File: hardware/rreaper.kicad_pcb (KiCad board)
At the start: 2 copper layers, 20 parts, among them J1 ZIF, J2 USB_B_Micro, J3 ICP, U1 ATmega328P, U2 MCP2221A, U3 74HC595, U4 74HC595, X1 16MHz

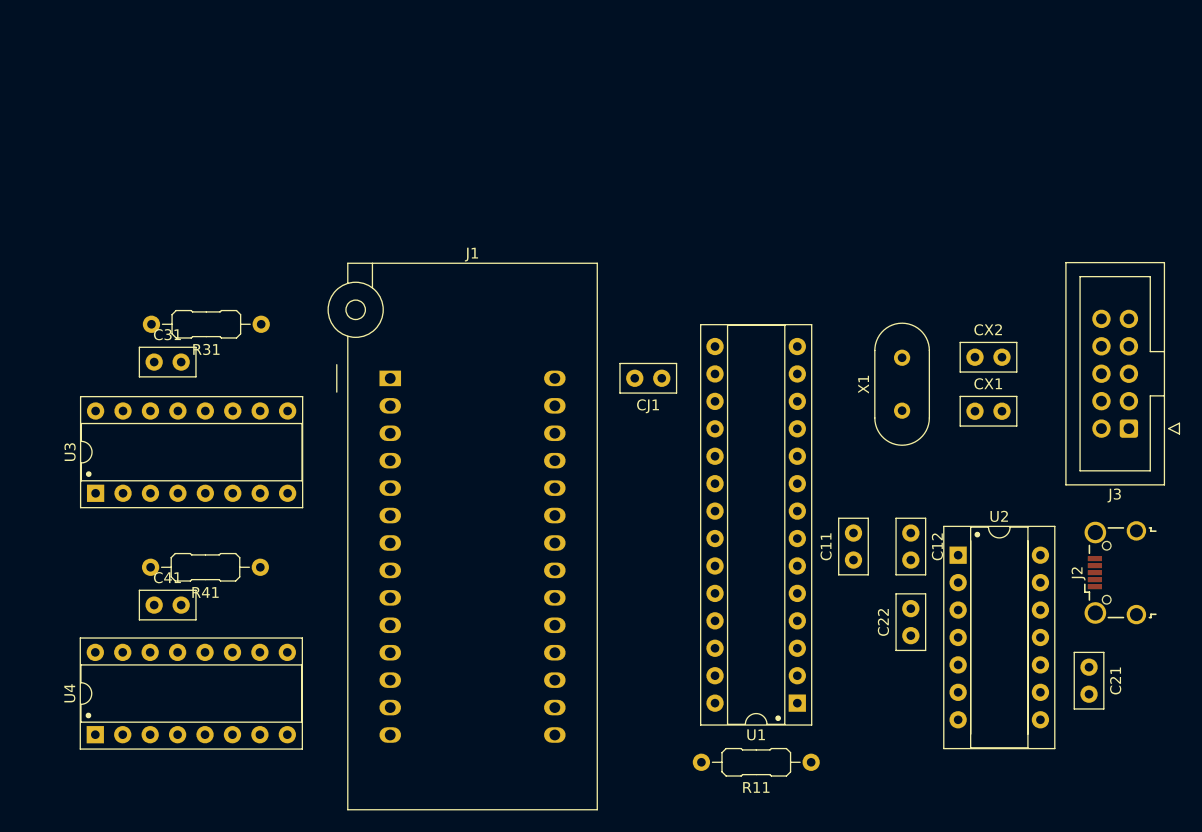
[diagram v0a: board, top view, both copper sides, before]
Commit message: completed first PCB layout
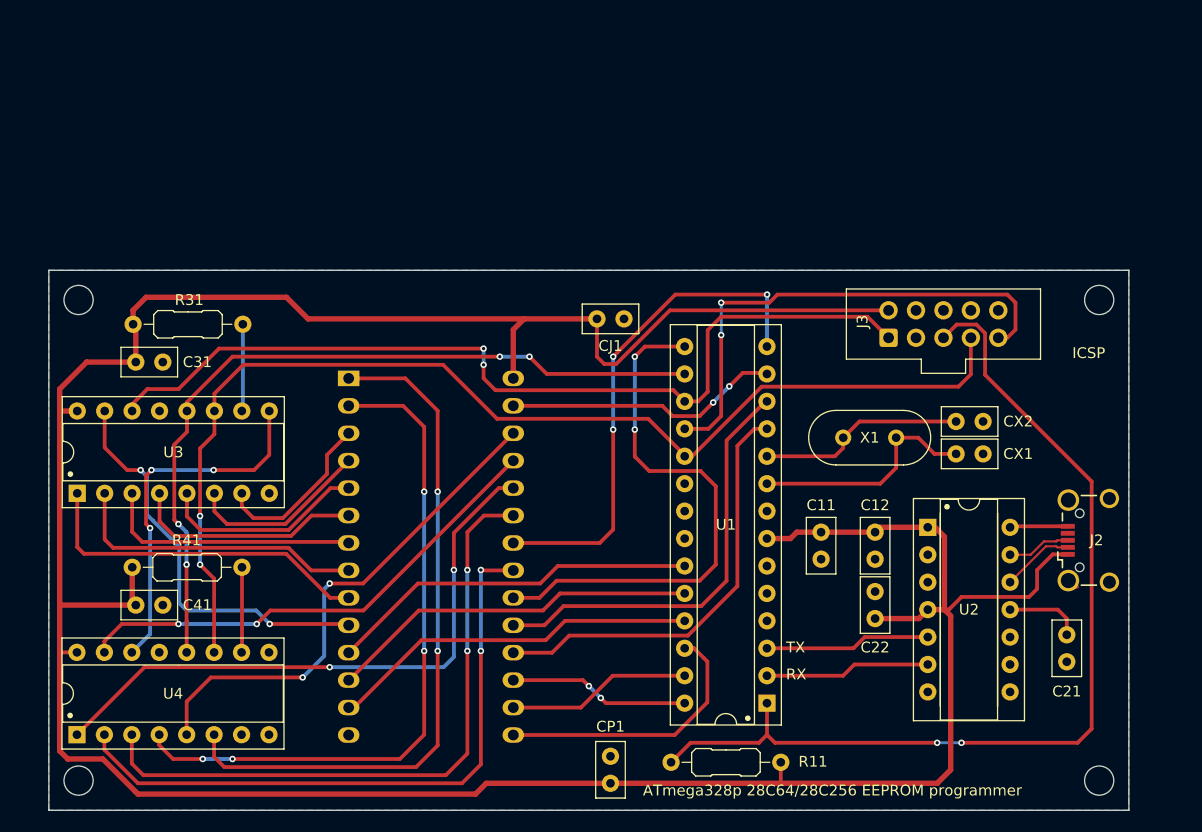
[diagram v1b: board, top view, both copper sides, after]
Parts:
- added CP1: 1u, Capacitor_THT:C_Disc_D5.0mm_W2.5mm_P2.50mm, F.Cu at (129.5, 118.0)
- added H1: MountingHole, MountingHole:MountingHole_2.7mm_M2.5, F.Cu at (174.8, 75.8)
- added H2: MountingHole, MountingHole:MountingHole_2.7mm_M2.5, F.Cu at (174.8, 120.2)
- added H3: MountingHole, MountingHole:MountingHole_2.7mm_M2.5, F.Cu at (80.2, 120.2)
- added H4: MountingHole, MountingHole:MountingHole_2.7mm_M2.5, F.Cu at (80.2, 75.8)
- J3: value ICP -> ICSP
- moved J3 23.8 mm to (155.2, 79.2), turned to 90 degrees
- moved CJ1 6.52 mm to (130.8, 77.5)
- moved CX2 6.20 mm to (161.5, 87.0)
- moved CX1 4.32 mm to (161.5, 90.0)
- moved C11 3.96 mm to (149.0, 97.2), turned to -90 degrees
- moved J2 3.91 mm to (173.7, 98.0)
- moved J1 3.85 mm to (105.3, 83.0)
- moved U2 3.81 mm to (158.9, 96.8)
- moved C22 3.67 mm to (154.0, 105.2)
- moved C21 3.64 mm to (171.8, 106.8)
- moved C12 3.31 mm to (154.0, 97.2)
- moved R11 2.81 mm to (145.3, 118.6)
- moved U1 2.81 mm to (144.0, 113.1)
- moved X1 2.56 mm to (155.9, 88.5), turned to 180 degrees
- moved C31 1.70 mm to (85.5, 81.5)
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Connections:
- net Net-(J2-D+) renamed /USB+
- net Net-(J2-D-) renamed /USB-
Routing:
- net +5V: track 0.00 -> 291.0 mm
- net SCK: track 0.00 -> 106.3 mm, vias 0 -> 2
- net ~{RST}: track 0.00 -> 89.2 mm, vias 0 -> 2
- net MOSI: track 0.00 -> 83.8 mm, vias 0 -> 2
- net LATCH: track 0.00 -> 72.6 mm, vias 0 -> 4
- net A14: track 0.00 -> 64.5 mm, vias 0 -> 2
- net A12: track 0.00 -> 63.3 mm, vias 0 -> 4
- net A11: track 0.00 -> 60.4 mm, vias 0 -> 2
- net A10: track 0.00 -> 59.3 mm, vias 0 -> 2
- net A9: track 0.00 -> 56.6 mm, vias 0 -> 2
- net CE: track 0.00 -> 50.2 mm, vias 0 -> 2
- net A13: track 0.00 -> 47.2 mm, vias 0 -> 2
- net OE: track 0.00 -> 47.2 mm, vias 0 -> 3
- net MISO: track 0.00 -> 46.6 mm, vias 0 -> 2
- net A8: track 0.00 -> 45.8 mm, vias 0 -> 2
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- added copper zone on B.Cu, net GND
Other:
- board outline added: 100 x 50 mm
- board text added: "ATmega328p 28C64/28C256 EEPROM programmer"
- board text added: "ICSP"
- board text added: "RX"
- board text added: "TX"

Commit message: hardware: replaced USB with RS485 and external power; redesigned PCB
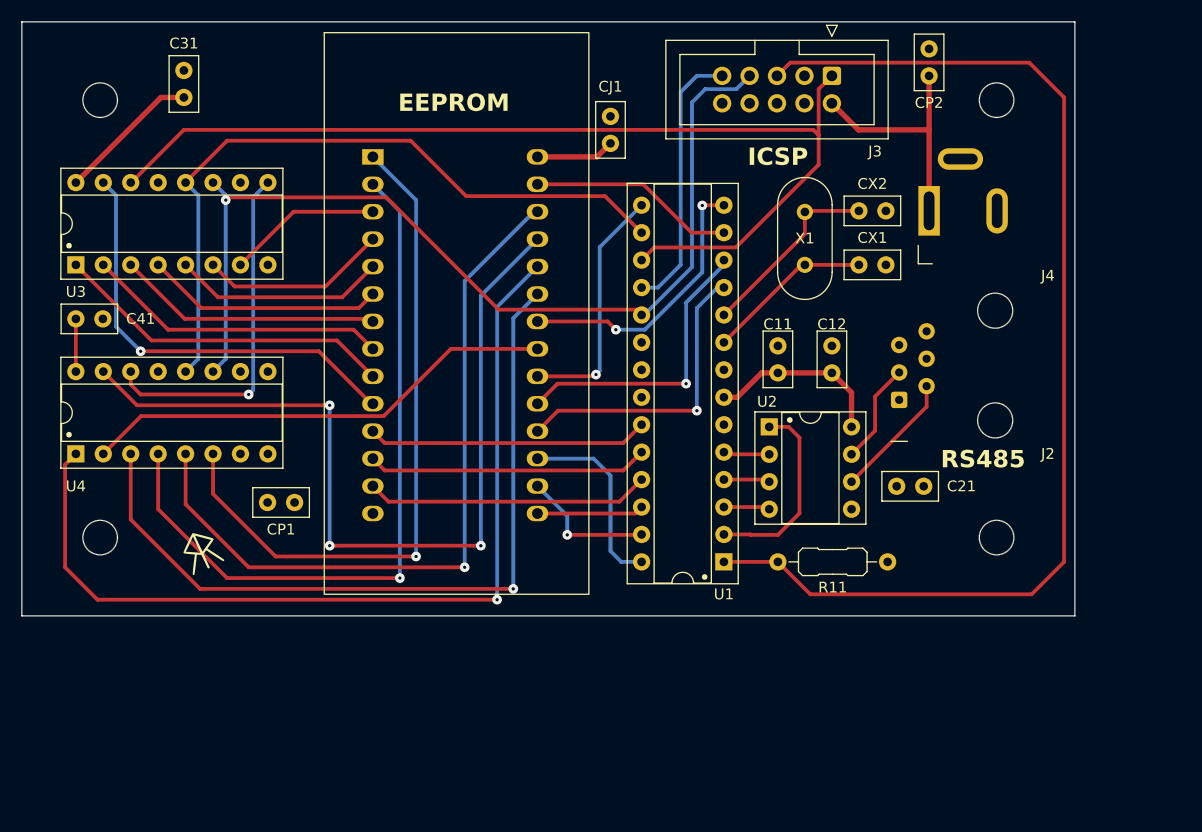
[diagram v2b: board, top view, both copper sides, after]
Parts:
- removed C22: 100n, Capacitor_THT:C_Disc_D5.0mm_W2.5mm_P2.50mm
- removed R31, R41: 4k7, PCM_Resistor_THT_AKL:R_Axial_DIN0207_L6.3mm_D2.5mm_P10.16mm_Horizontal
- added CP2: 1u, Capacitor_THT:C_Disc_D5.0mm_W2.5mm_P2.50mm, F.Cu at (159.0, 52.5)
- added G***: LOGO, LOGO, F.Cu at (91.5, 99.0)
- added G***: LOGO, LOGO, B.Cu at (127.0, 52.5)
- added J4: 5V_{DC}, Connector_BarrelJack:BarrelJack_GCT_DCJ200-10-A_Horizontal, F.Cu at (159.0, 67.5)
- C21: value 220n -> 100n
- H1, H2, H3, H4: footprint MountingHole:MountingHole_2.7mm_M2.5 -> MountingHole:MountingHole_3.2mm_M3
- J2: value USB_B_Micro -> RS485; footprint Connector_USB:USB_Micro-B_Wuerth_629105150521_CircularHoles -> Connector_RJ:RJ12_Amphenol_54601-x06_Horizontal
- U2: value MCP2221A -> SN75176AP; footprint PCM_Package_DIP_AKL:DIP-14_W7.62mm_Socket -> PCM_Package_DIP_AKL:DIP-8_W7.62mm_Socket
- moved H2 95.2 mm to (82.2, 97.8)
- moved H1 94.3 mm to (82.2, 57.2)
- moved H3 87.9 mm to (165.2, 97.8)
- moved H4 87.0 mm to (165.2, 57.2)
- moved CP1 37.5 mm to (100.2, 94.5), turned to 180 degrees
- moved C41 27.1 mm to (80.0, 77.5)
- moved U4 26.0 mm to (80.0, 90.0)
- moved C31 24.9 mm to (90.0, 57.0), turned to 90 degrees
- moved J3 24.8 mm to (150.0, 55.0), turned to -90 degrees
- moved J2 21.8 mm to (156.2, 85.0)
- moved CX2 21.5 mm to (152.5, 67.5)
- moved U3 21.2 mm to (80.0, 72.5)
- moved R11 21.0 mm to (155.2, 100.0)
- moved C21 20.9 mm to (156.0, 93.0), turned to 0 degrees
- moved J1 20.6 mm to (107.5, 62.5)
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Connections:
- C21 pad 1: Net-(U2-VUSB) -> +5V
- J2 pad 1: +5V -> GND
- J2 pad 2: /USB- -> SA
- J2 pad 3: /USB+ -> SB
- J2 pad 5: GND -> unconnected-(J2-Pad5)
- U1 pad 2: UART_{PC->MCU} -> RX
- U1 pad 3: UART_{MCU->PC} -> TX
- U1 pad 4: unconnected-(U1-PD2-Pad4) -> DE
- U1 pad 5: unconnected-(U1-PD3-Pad5) -> ~{RE}
- U2 pad 1: +5V -> RX
- U2 pad 2: unconnected-(U2-GP0-Pad2) -> ~{RE}
- U2 pad 3: unconnected-(U2-GP1-Pad3) -> DE
- U2 pad 4: +5V -> TX
- U2 pad 5: UART_{MCU->PC} -> GND
- U2 pad 6: UART_{PC->MCU} -> SA
- U2 pad 7: unconnected-(U2-GP2-Pad7) -> SB
- U2 pad 8: unconnected-(U2-GP3-Pad8) -> +5V
- U3 pad 10: Net-(U3-~{SRCLR}) -> +5V
- U4 pad 10: Net-(U4-~{SRCLR}) -> +5V
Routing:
- net +5V: track 291.0 -> 64.6 mm
- net A8: track 45.8 -> 79.8 mm, vias 2 -> 3
- net A9: track 56.6 -> 84.7 mm, vias 2 -> 1
- net CE: track 50.2 -> 22.9 mm, vias 2 -> 1
- net MISO: track 46.6 -> 24.9 mm, vias 2 -> 0
- net A13: track 47.2 -> 68.8 mm, vias 2 -> 1
- net OE: track 47.2 -> 26.0 mm, vias 3 -> 2
- net RX: track 0.00 -> 18.1 mm
- net SCK: track 106.3 -> 89.6 mm, vias 2 -> 1
- net ~{RST}: track 89.2 -> 105.4 mm, vias 2 -> 0
- net D3: track 25.6 -> 9.89 mm
- net UART_{MCU->PC}: track 15.6 -> 0.00 mm
- net UART_{PC->MCU}: track 15.3 -> 0.00 mm
- net A10: track 59.3 -> 44.2 mm, vias 2 -> 0
- net D7: track 39.7 -> 27.4 mm, vias 0 -> 1
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- added copper zone on In1.Cu, net +5V
- added copper zone on In2.Cu, net GND
- removed copper zone on B.Cu, net GND
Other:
- board size 100 x 50 mm -> 97.5 x 55 mm
- copper layers 2 -> 4
- board text added: "5V"
- board text added: "COMPATIBLE DEVICES: AT28C64 AT28C256"
- board text added: "EEPROM"
- board text added: "RS485"
- board text added: "RS485: 1 GND 2 A 3 B ... X"
- board text removed: "ATmega328p 28C64/28C256 EEPROM programmer"
- board text removed: "RX"
- board text removed: "TX"

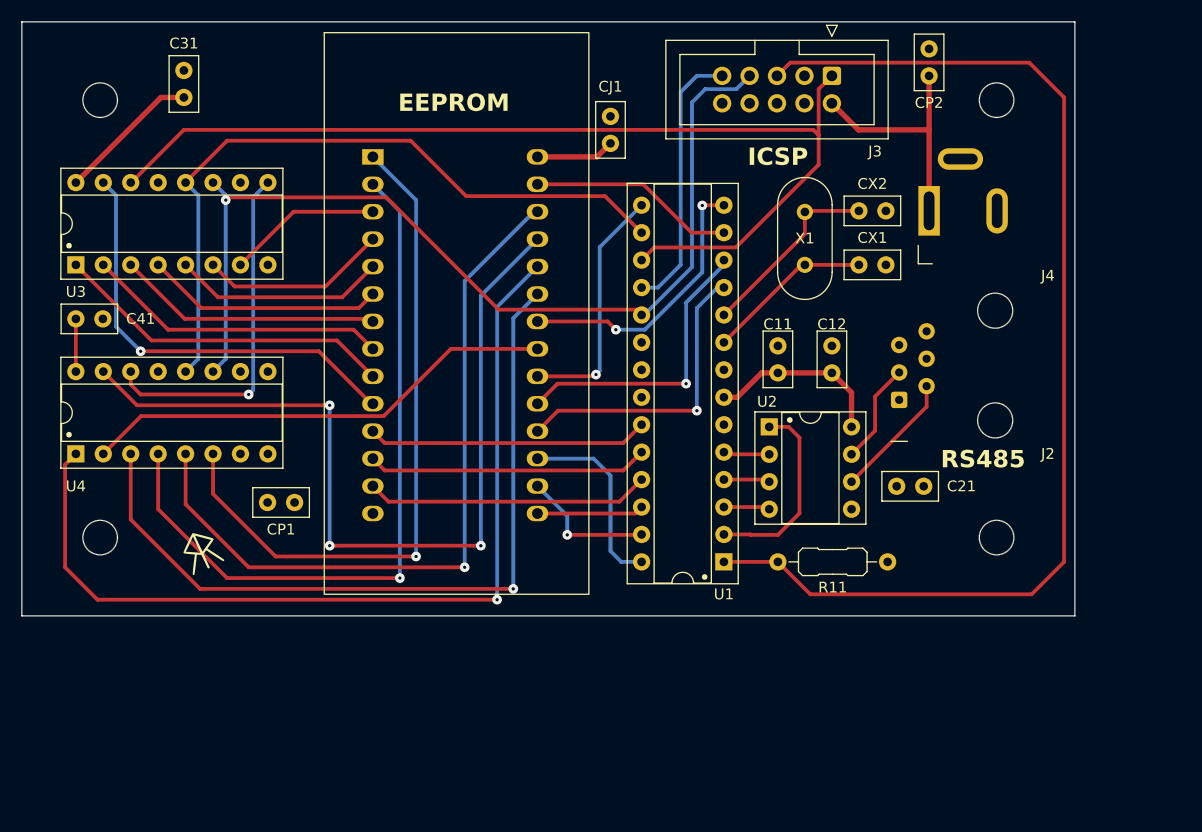
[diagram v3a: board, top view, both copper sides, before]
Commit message: went back to USB; added serial eeprom socket; completed new layout
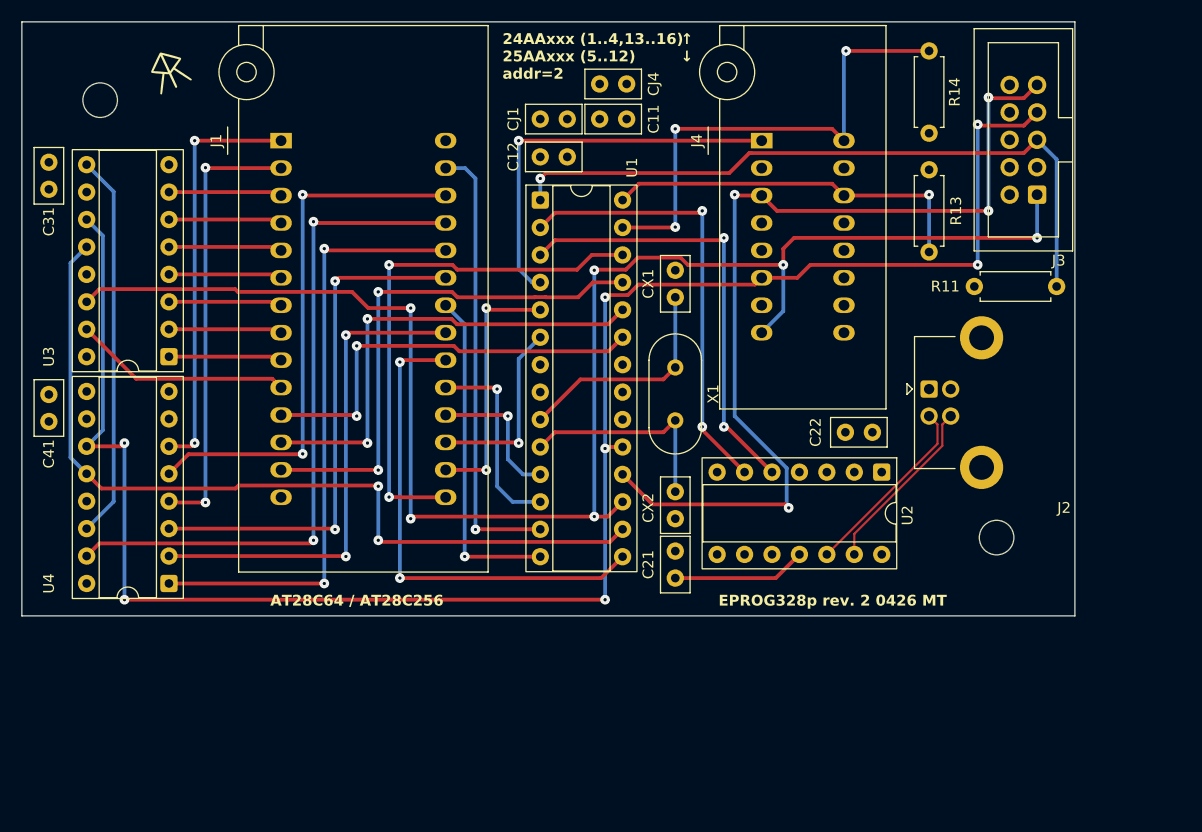
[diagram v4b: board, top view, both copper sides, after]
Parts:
- removed CP1, CP2: 1u, Capacitor_THT:C_Disc_D5.0mm_W2.5mm_P2.50mm
- removed the G*** at (127.0, 52.5)
- removed H2, H4: MountingHole, MountingHole:MountingHole_3.2mm_M3
- added C22: 100n, Capacitor_THT:C_Disc_D5.0mm_W2.5mm_P2.50mm, F.Cu at (153.8, 88.0)
- added CJ4: 100n, Capacitor_THT:C_Disc_D5.0mm_W2.5mm_P2.50mm, F.Cu at (131.0, 55.8)
- added R13: 4k7, Resistor_THT:R_Axial_DIN0207_L6.3mm_D2.5mm_P7.62mm_Horizontal, F.Cu at (159.0, 71.3)
- added R14: 4k7, Resistor_THT:R_Axial_DIN0207_L6.3mm_D2.5mm_P7.62mm_Horizontal, F.Cu at (159.0, 52.7)
- C21: value 100n -> 220n
- J1: value ZIF -> ZIF28; footprint Socket:DIP_Socket-28_W11.9_W12.7_W15.24_W17.78_W18.5_3M_228-1277-00-0602J -> Socket:DIP_Socket-28_W11.9mm_W12.7mm_W15.24mm_W17.78mm_W18.5mm_3M_228-1277-00-0602J
- J2: value RS485 -> USB_B; footprint Connector_RJ:RJ12_Amphenol_54601-x06_Horizontal -> Connector_USB:USB_B_Lumberg_2411_02_Horizontal
- J4: value 5V_{DC} -> ZIF16; footprint Connector_BarrelJack:BarrelJack_GCT_DCJ200-10-A_Horizontal -> Socket:DIP_Socket-16_W4.3mm_W5.08mm_W7.62mm_W10.16mm_W10.9mm_3M_216-3340-00-0602J
- R11: footprint PCM_Resistor_THT_AKL:R_Axial_DIN0207_L6.3mm_D2.5mm_P10.16mm_Horizontal -> Resistor_THT:R_Axial_DIN0207_L6.3mm_D2.5mm_P7.62mm_Horizontal
- U1: footprint PCM_Package_DIP_AKL:DIP-28_W7.62mm_Socket -> Package_DIP:DIP-28_W7.62mm_Socket
- U2: value SN75176AP -> MCP2221A; footprint PCM_Package_DIP_AKL:DIP-8_W7.62mm_Socket -> Package_DIP:DIP-14_W7.62mm_Socket
- U3, U4: footprint PCM_Package_DIP_AKL:DIP-16_W7.62mm_Socket -> Package_DIP:DIP-16_W7.62mm_Socket
- moved G*** 44.6 mm to (88.5, 54.5)
- moved U1 37.6 mm to (123.0, 66.5), turned to 0 degrees
- moved C12 33.6 mm to (123.0, 62.5), turned to 0 degrees
- moved CX2 31.1 mm to (135.5, 93.5), turned to -90 degrees
- moved C11 28.7 mm to (128.5, 59.0), turned to 0 degrees
- moved R11 26.7 mm to (163.2, 74.5), turned to 0 degrees
- moved C21 22.2 mm to (135.5, 101.5), turned to 90 degrees
- moved J3 22.0 mm to (169.0, 66.0), turned to 180 degrees
- moved CX1 17.3 mm to (135.5, 75.5), turned to 90 degrees
- moved J4 16.8 mm to (143.5, 61.0), turned to 0 degrees
- moved X1 15.3 mm to (135.5, 82.0), turned to -90 degrees
- moved C31 15.1 mm to (77.5, 65.5)
- moved U4 14.8 mm to (88.6, 102.0), turned to 180 degrees
- moved U3 12.1 mm to (88.6, 81.0), turned to 180 degrees
- moved U2 11.2 mm to (154.6, 91.7), turned to -90 degrees
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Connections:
- net Net-(U3-QH') renamed /CARRY
- C21 pad 1: +5V -> Net-(U2-VUSB)
- J2 pad 1: GND -> +5V
- J2 pad 2: SA -> /USB-
- J2 pad 3: SB -> /USB+
- J2 pad 4: unconnected-(J2-Pad4) -> GND
- J4 pad 1: +5V -> ~{CS}
- J4 pad 2: GND -> +5V
- J4 pad 3: (no net) -> MISO
- U1 pad 27: D4 -> SDA
- U1 pad 28: D5 -> SCL
- U1 pad 4: DE -> ~{CS}
- U1 pad 5: ~{RE} -> D4
- U1 pad 6: unconnected-(U1-PD4-Pad6) -> D5
- U2 pad 1: RX -> +5V
- U2 pad 2: ~{RE} -> unconnected-(U2-GP0-Pad2)
- U2 pad 3: DE -> unconnected-(U2-GP1-Pad3)
- U2 pad 4: TX -> +5V
- U2 pad 5: GND -> TX
- U2 pad 6: SA -> RX
- U2 pad 7: SB -> unconnected-(U2-GP2-Pad7)
- U2 pad 8: +5V -> unconnected-(U2-GP3-Pad8)
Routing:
- net SCK: track 89.6 -> 169.3 mm, vias 1 -> 7
- net +5V: track 64.6 -> 0.00 mm
- net MISO: track 24.9 -> 87.4 mm, vias 0 -> 4
- net MOSI: track 94.7 -> 148.6 mm, vias 0 -> 6
- net SDA: track 0.00 -> 46.7 mm, vias 0 -> 3
- net ~{RST}: track 105.4 -> 63.8 mm, vias 0 -> 1
- net D3: track 9.89 -> 49.1 mm, vias 0 -> 2
- net TX: track 4.28 -> 41.3 mm, vias 0 -> 2
- net ~{CS}: track 0.00 -> 36.9 mm, vias 0 -> 1
- net SCL: track 0.00 -> 34.3 mm, vias 0 -> 1
- net A9: track 84.7 -> 56.7 mm, vias 1 -> 2
- net A12: track 67.6 -> 41.4 mm, vias 1 -> 2
- net A14: track 63.6 -> 38.5 mm, vias 1 -> 2
- net A11: track 72.5 -> 48.8 mm, vias 1 -> 2
- net RX: track 18.1 -> 41.4 mm, vias 0 -> 2
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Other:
- board text added: "24AAxxx (1..4,13..16) 25AAxxx (5..12) addr=2"
- board text added: "AT28C64 / AT28C256"
- board text added: "EPROG328p rev. 2 0426 MT"
- board text added: "↑ ↓"
- board text removed: "5V"
- board text removed: "COMPATIBLE DEVICES: AT28C64 AT28C256"
- board text removed: "EEPROM"
- board text removed: "ICSP"
- board text removed: "RS485"
- board text removed: "RS485: 1 GND 2 A 3 B ... X"
